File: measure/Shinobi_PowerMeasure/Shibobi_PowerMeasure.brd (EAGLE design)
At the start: 40.5 x 35 mm, 28 parts, among them M1 MCP73871

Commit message: Solar Add resistance constant,PowerMeasure
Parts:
- removed DC: 4UCON-DC, FaBo-Supply:4UCON-DC
- removed LIPO, SYS: FABO_BRICK_2PIN_SIDE, FaBo-Template:FABO_BRICK_2PIN_S02B−PASK-2_SILK
- removed M1: MCP73871, FaBo-Solar:QFN
- removed PG, STAT1, STAT2: (no value), FaBo-LED:0603
- removed SJ1: OPEN, FaBo-etc:SMD-JUMPER-2
- removed U$1: (no value), FaBo-Logo:LOGO_FABO_S
- added C10: 0.1uF, FaBo-Capacitor:0603
- added C6: 1uF, FaBo-Capacitor:0603
- added C7: NC, FaBo-Capacitor:0603
- added C8, C9: 10uF, FaBo-Capacitor:0603
- added D2: MBR0520L, FaBo:MBR0502L
- added IC1: 3.3V, FaBo-Supply:SOT-23-5
- added ISO: ISO1541, FaBo:ISO1541
- added J1: (no value), FaBo-Template:FABO_BRICK_I2C_S04B-PASK-2
- added LED1: RED, FaBo-LED:0603
- added LED2: GREEN, FaBo-LED:0603
- added LED3: BLUE, FaBo-LED:0603
- added R12: 1KΩ, FaBo-Resistors:0603
- added R13, R14: 4.7KΩ, FaBo-Resistors:0603
- added R15: 510Ω, FaBo-Resistors:0603
- added R16: 1Ω, FaBo-Resistors:0603
- added R17, R18, R19: NC, FaBo-Resistors:0603
- added S1: 219-08J, switch-dil:CTS-219-08J
- added SHUNT1: PMR10EZPFV2L00, FaBo:PMR10EZPFV2L00
- added SHUNT2: WSL2010R0250FEB, FaBo:WSL2010R0250FEB
- added T1: (no value), transistor:SC59-BEC
- added T2: 760390014, FaBo:760390014
- added TP1, TP2: TPPAD1-17, testpad:P1-17
- added U$3: ML-1400-S1, FaBo-Terminal:ML-1400-S1
- added U$5: (no value), FaBo-Template:FABO-SHINOBI
- added U$6: (no value), FaBo-Logo:LOGO_FABO_S
- added U$8: TPS76333, FaBo:TPS76333
- added U1: SN6501DBVR, TI:SOT-23-5
- added U2: TI-INA226, FaBo-Sensor:TI-INA226
- C1: value 10uf -> 0.1uF
- C2, C3: value 4.7uf -> 0.1uF
- C4: value 1uF -> 0.1uF
- C5: value NC -> 10uF; device rcl:E5-13 -> FaBo-Capacitor:0603
- D1: value DIODEDO-214AC -> MBR0520L; device FaBo-Diode:DO-214AC -> FaBo:MBR0502L
- IC2: device FaBo-Supply:SOT-23-5 -> FaBo-LevelTranslator:XQFN8
- R1: value 470 -> 4.7KΩ
- R10: value NTC Thermistor 10K -> 0Ω; device FaBo-Resistors:AXL-REGULAR -> FaBo-Resistors:0603
- R11: value 0 -> 0Ω
- R2: value 470 -> 1KΩ
- R3: value 470 -> NC
- R4: value 10K -> NC
- R5: value 10K -> 4.7KΩ
- R6: value 150K -> 4.7KΩ
- R7: value 270K -> 10Ω
- R8: value 100K -> 10Ω
- R9: value 240 -> 200KΩ
- U$2: value (none) -> ML-1400-S1; device FaBo-Template:FABO-SHINOBI -> FaBo-Terminal:ML-1400-S1
- moved R3 33.2 mm to (2.67, 23.1), flipped to the bottom, turned to 270 degrees
- moved R10 30.5 mm to (10.5, 28.6), flipped to the bottom, turned to 180 degrees
- moved U$2 30.3 mm to (10.3, 28.4)
- moved R11 26.8 mm to (20.4, 28.4), flipped to the bottom
- moved R2 26.5 mm to (8.64, 17.5), turned to 0 degrees
- moved C4 22.0 mm to (19.3, 4.70), flipped to the bottom, turned to 0 degrees
- moved R4 20.0 mm to (4.45, 23.1), flipped to the bottom, turned to 270 degrees
- moved R6 17.6 mm to (28.3, 25.9)
- moved R7 17.2 mm to (30.7, 19.4), flipped to the bottom, turned to 90 degrees
- moved R9 14.4 mm to (14.5, 10.7), flipped to the bottom, turned to 270 degrees
- moved IC2 14.2 mm to (18.2, 11.8), flipped to the bottom, turned to 270 degrees
- moved C1 13.9 mm to (27.4, 17.0), flipped to the bottom, turned to 180 degrees
- moved R1 13.1 mm to (22.1, 2.92), flipped to the bottom, turned to 270 degrees
- moved R5 12.9 mm to (28.2, 28.6)
- moved C5 11.9 mm to (3.05, 14.7)
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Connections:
- removed net LIPO_VCC: C2.2, LIPO.VCC, M1.P14, M1.P15, M1.P16
- removed net N$6: M1.P13, R4.1
- removed net SOLAR_VCC: C1.2, C5.+, D1.ANODE, M1.P17, M1.P18, M1.P19, M1.P3, M1.P4, PG.ANODE, R7.2, SJ1.1, STAT1.ANODE, STAT2.ANODE
- removed net SYS_VCC: C3.2, IC2.1, IC2.3, M1.P1, M1.P20
- removed net SYS_VCC_3V3: C4.2, IC2.5, SYS.VCC
- removed net TE: M1.P9, R11.2, SJ1.2
- removed net VPCC: M1.P2, R7.1, R8.2
- new net 3.3V: C2.2, C5.2, ISO.VCC2, R1.2, R2.1, R3.2, R5.1, R6.1, S1.11, S1.15, T1.E, U$8.OUT, U2.6
- new net A0: S1.1, S1.2, S1.3, S1.4, U2.2
- new net A1: S1.5, S1.6, S1.7, S1.8, U2.1
- new net GND_SECONDARY: C10.2, C2.1, C9.2, ISO.GND2, LED1.CATHODE, LED2.CATHODE, R11.2, R16.2, R4.2, S1.12, S1.16, T2.5, TP2.TP, U$3.RIGHT1, U$3.RIGHT2, U$8.GND, U2.7
- new net N$14: D1.P$2, T2.6
- new net N$15: D2.P$2, T2.4
- new net N$16: C10.1, C9.1, D1.P$1, D2.P$1, TP1.TP, U$8.EN, U$8.IN
- new net N$18: C4.2, IC2.7, IC2.8, R9.2
- new net N$19: C3.2, C8.2, IC1.1, IC1.3, J1.VCC, R12.1, R19.2, R9.1, T2.2, U1.2
- new net N$20: R3.1, R4.1, U$8.NC/FB
- new net N$21: C5.1, R16.1
- new net N$22: IC2.5, J1.SDA, R18.1
- new net N$23: IC2.3, ISO.SCL1, R13.1, R17.2
- new net N$7: LED1.ANODE, R15.1
- new net N$9: R15.2, T1.C
- new net SCL: ISO.SCL2, R6.2, S1.13, S1.9, U2.5
- new net SDA: ISO.SDA2, R5.2, S1.10, S1.14, U2.4
- new net VBUS: R10.1, U$2.LEFT1, U$2.LEFT2, U2.8
- new net VIN+: R10.2, R7.2, SHUNT1.P$2, SHUNT2.P$2, U$2.RIGHT1, U$2.RIGHT2
- new net VIN-: R11.1, R8.2, SHUNT1.P$1, SHUNT2.P$1, U$3.LEFT1, U$3.LEFT2
- net GND: now also C6.2, C7.2, C8.1, IC1.2, IC2.1, ISO.GND1, J1.GND, LED3.CATHODE, U1.4, U1.5; no longer C1.1, C2.1, C5.-, DC.GND1, IC2.2, LIPO.GND, M1.P$1, M1.P10, M1.P11, R10.1, R11.1, R4.2, R5.2, R6.1, R8.1, SYS.GND
- net N$1: now also C1.2, R7.1, U2.10; no longer PG.CATHODE, R1.1
- net N$10: now also LED3.ANODE, R12.2; no longer D1.CATHODE, DC.VCC
- net N$11: now also IC2.4, ISO.SDA1, R14.1, R18.2; no longer M1.P6, R1.2
- net N$12: now also IC2.6, J1.SCL, R17.1; no longer M1.P7, R2.2
- net N$13: now also C6.1, C7.1, IC1.5, IC2.2, ISO.VCC1, R13.2, R14.2, R19.1; no longer M1.P8, R3.2
- net N$2: now also C1.1, R8.1, U2.9; no longer R2.1, STAT2.CATHODE
- net N$3: now also T2.1, U1.3; no longer M1.P5, R9.1
- net N$4: now also T2.3, U1.1; no longer M1.P12, R5.1
- net N$5: now also R1.1, T1.B, U2.3; no longer R10.2, R6.2, R9.2
- net N$8: now also LED2.ANODE, R2.2; no longer R3.1, STAT1.CATHODE
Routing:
- net GND_SECONDARY: track 0.00 -> 109.4 mm, vias 0 -> 2
- net 3.3V: track 0.00 -> 104.5 mm, vias 0 -> 13
- net N$19: track 0.00 -> 75.8 mm, vias 0 -> 6
- net GND: track 0.00 -> 75.6 mm, vias 5 -> 3
- net SOLAR_VCC: track 71.5 -> 0.00 mm, vias 4 -> 0
- net SDA: track 0.00 -> 57.5 mm, vias 0 -> 3
- net SCL: track 0.00 -> 55.1 mm, vias 0 -> 7
- net VIN+: track 0.00 -> 40.6 mm
- net VBUS: track 0.00 -> 33.5 mm
- net TE: track 27.6 -> 0.00 mm
- net VIN-: track 0.00 -> 27.5 mm
- net N$16: track 0.00 -> 26.3 mm, vias 0 -> 2
- net A1: track 0.00 -> 25.7 mm, vias 0 -> 3
- net A0: track 0.00 -> 24.6 mm, vias 0 -> 3
- net VPCC: track 20.7 -> 0.00 mm, vias 5 -> 0
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- added copper zone on layer 1, net GND_SECONDARY
- added copper zone on layer 16, net GND_SECONDARY
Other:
- outline, holes or cut-outs redrawn
- board text added: "#7"
- board text added: "A0"
- board text added: "A1"
- board text added: "GND"
- board text added: "IN+"
- board text added: "IN-"
- board text added: "ISO"
- board text added: "PowerMeasure"
- board text added: "Rev.1.0.0 A"
- board text added: "S-PM01"
- board text added: "SCL"
- board text added: "SDA"
- board text added: "TR"
- board text added: "VBUS"
- board text added: "VS"
- board text removed: "#3"
- board text removed: "LiPo"
- board text removed: "Rev. 1.0.1 C"
- board text removed: "SOLAR"
- board text removed: "SYS"
- board text removed: "Solar"

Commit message: Dimention Delete
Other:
- outline, holes or cut-outs redrawn
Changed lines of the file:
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@@
 <?xml version="1.0" encoding="utf-8"?>
 <!DOCTYPE eagle SYSTEM "eagle.dtd">
-<eagle version="8.7.0">
+<eagle version="8.7.1">
 <drawing>
 <settings>
-<setting alwaysvectorfont="no"/>
+<setting alwaysvectorfont="yes"/>
 <setting verticaltext="up"/>
 </settings>
@@
 <board>
 <plain>
-<wire x1="0" y1="0" x2="40.5" y2="0" width="0" layer="20"/>
-<wire x1="40.5" y1="0" x2="40.5" y2="35" width="0" layer="20"/>
-<wire x1="40.5" y1="35" x2="0" y2="35" width="0" layer="20"/>
-<wire x1="0" y1="35" x2="0" y2="0" width="0" layer="20"/>
 <text x="26.789" y="30.353" size="0.8128" layer="21">PowerMeasure</text>
 <text x="26.789" y="32.512" size="1.778" layer="21">#7</text>

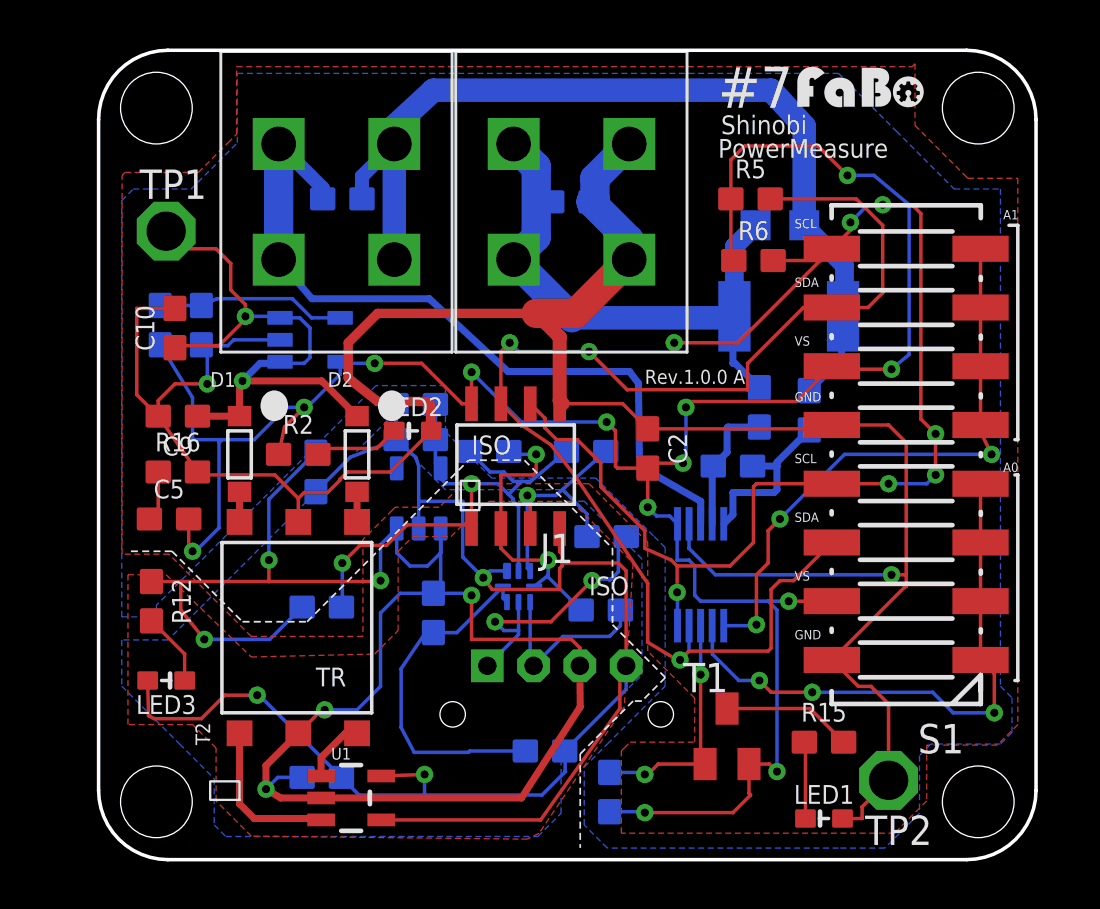
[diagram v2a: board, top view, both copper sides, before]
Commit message: Add silk printing Fixed garbled characters
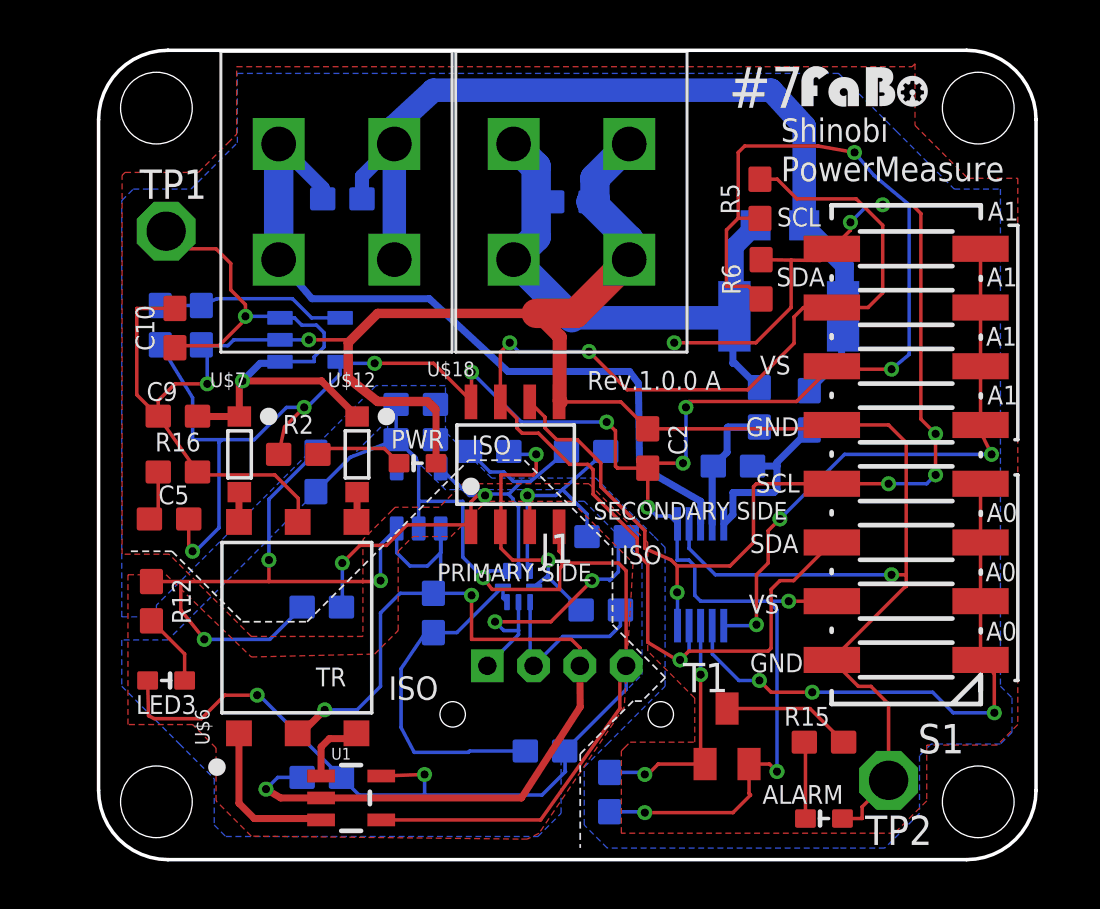
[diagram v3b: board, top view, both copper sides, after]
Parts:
- removed D1, D2: MBR0520L, FaBo:MBR0502L
- removed ISO: ISO1541, FaBo:ISO1541
- removed LED2: GREEN, FaBo-LED:0603
- removed T2: 760390014, FaBo:760390014
- added PWR: GREEN, FaBo-LED:0603
- added U$12, U$7: MBR0520L, FaBo:MBR0502L
- added U$18: ISO1541, FaBo:ISO1541
- added U$19: (no value), FaBo-Logo:LOGO_FABO_S
- U$6: value (none) -> 760390014; device FaBo-Logo:LOGO_FABO_S -> FaBo:760390014
- moved U$6 33.1 mm to (8.61, 10.0), turned to 90 degrees
- moved R6 0.88 mm to (28.7, 25.1), turned to 90 degrees
- moved R5 0.41 mm to (28.6, 28.6), turned to 90 degrees
- renumbered LED1 to ALARM
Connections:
- removed net N$15: D2.P$2, T2.4
- new net N$6: U$6.6, U$7.P$2
- net 3.3V: now also U$18.VCC2; no longer ISO.VCC2
- net GND: now also U$18.GND1; no longer ISO.GND1
- net GND_SECONDARY: now also PWR.CATHODE, U$18.GND2, U$6.5; no longer ISO.GND2, LED2.CATHODE, T2.5
- net N$11: now also U$18.SDA1; no longer ISO.SDA1
- net N$13: now also U$18.VCC1; no longer ISO.VCC1
- net N$14: now also U$12.P$2, U$6.4; no longer D1.P$2, T2.6
- net N$16: now also U$12.P$1, U$7.P$1; no longer D1.P$1, D2.P$1
- net N$19: now also U$6.2; no longer T2.2
- net N$23: now also U$18.SCL1; no longer ISO.SCL1
- net N$3: now also U$6.1; no longer T2.1
- net N$4: now also U$6.3; no longer T2.3
- net N$8: now also PWR.ANODE; no longer LED2.ANODE
- net SCL: now also U$18.SCL2; no longer ISO.SCL2
- net SDA: now also U$18.SDA2; no longer ISO.SDA2
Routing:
- net 3.3V: track 104.5 -> 108.0 mm
- net N$19: track 75.8 -> 72.9 mm
- net GND_SECONDARY: track 109.4 -> 106.9 mm, vias 2 -> 3
- net SDA: track 57.5 -> 59.5 mm
- net N$15: track 1.30 -> 0.00 mm
- net N$6: track 0.00 -> 1.30 mm
- net N$16: track 26.3 -> 27.5 mm
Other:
- board text added: "0x40 0x41 0x42 0x43 0x44 0x45 0x46 0x47"
- board text added: "A0 | A1 | ADDRESS GND GND GND VS GND SDA GND SCL VS GND VS VS VS SDA VS SCL"
- board text added: "PRIMARY SIDE"
- board text added: "SECONDARY SIDE"
